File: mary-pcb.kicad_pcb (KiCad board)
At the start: 2 copper layers, 76.2 x 130.8 mm, 69 parts, among them SW1 SW_Push, SW2 Rotary_Encoder_Switch, U1 ATmega32U4-AU, Y1 16MHz

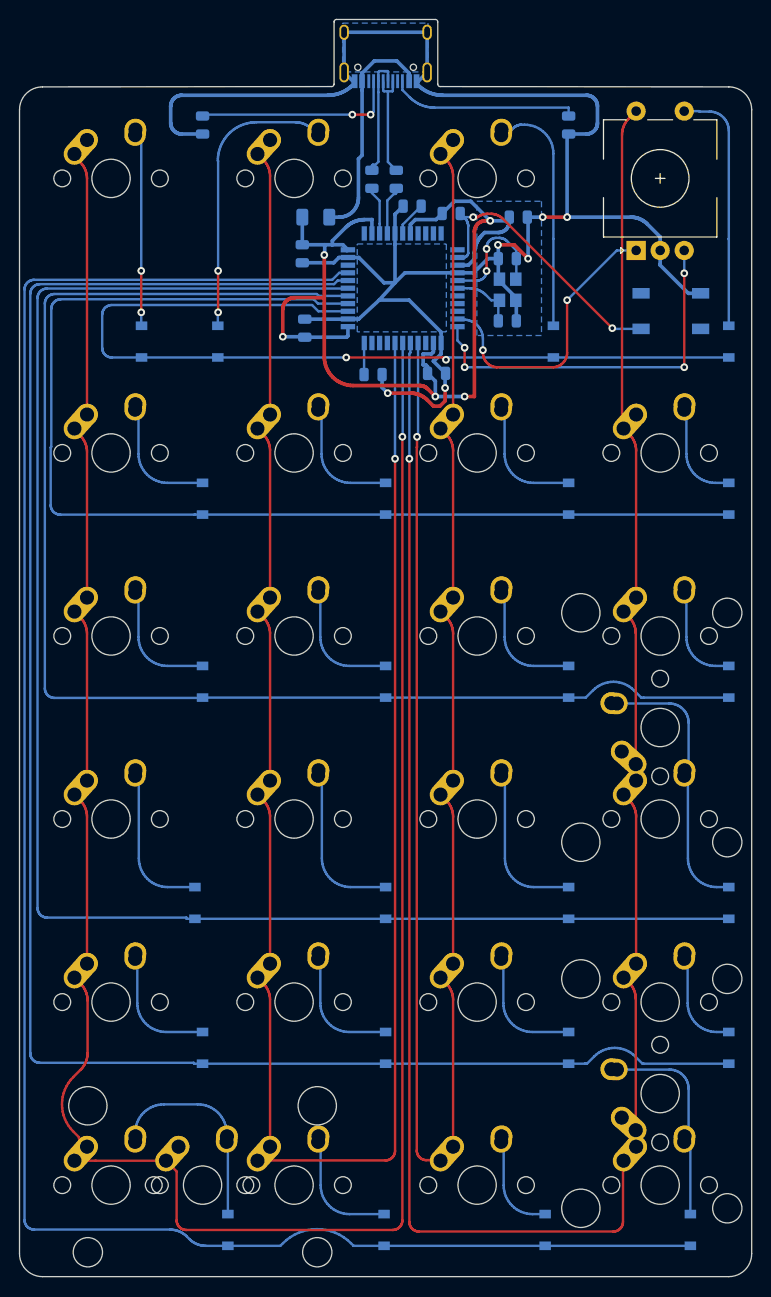
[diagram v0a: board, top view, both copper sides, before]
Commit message: add esd protection, ground pours, via stitching
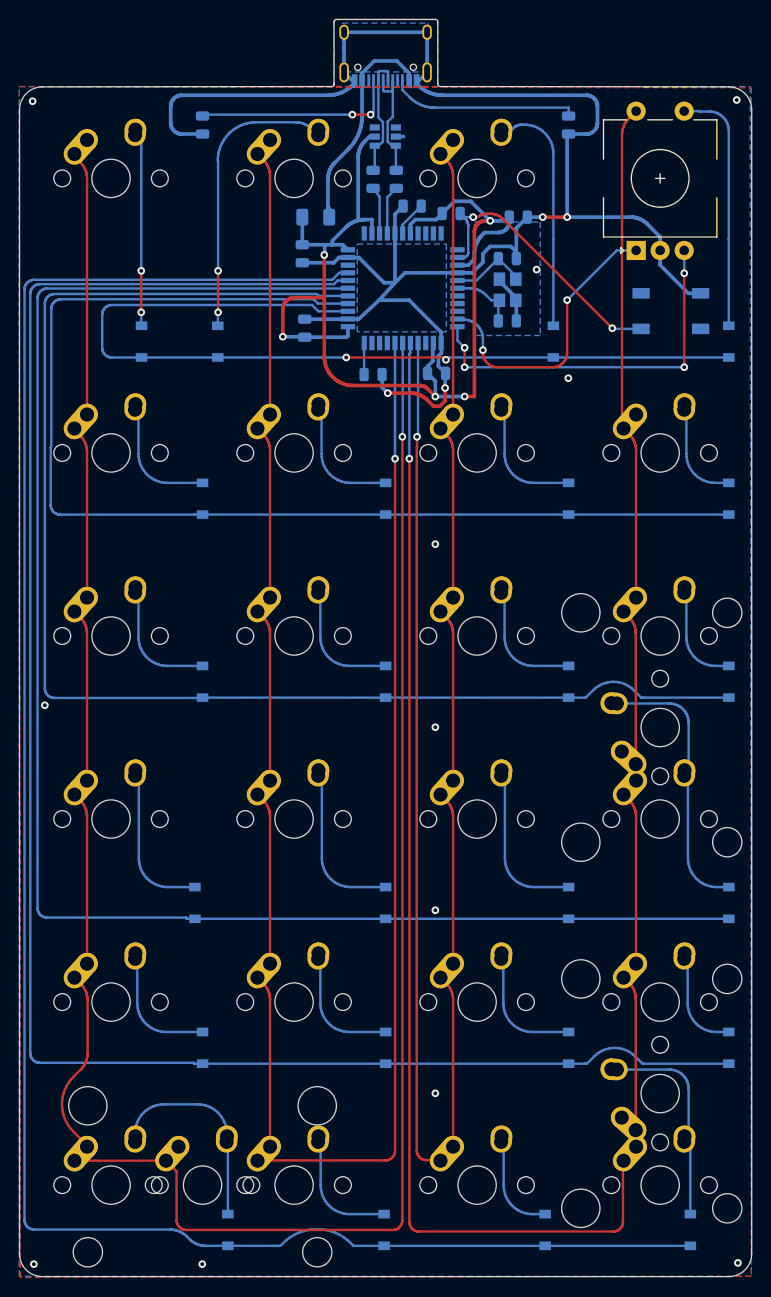
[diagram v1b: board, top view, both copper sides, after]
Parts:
- added U2: SRV05-4, Package_TO_SOT_SMD:SOT-23-6, B.Cu at (153.2, 37.7)
- moved R5 0.13 mm to (151.9, 42.2)
- turned C2 to 0 degrees
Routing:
- net +5V: track 108.7 -> 117.3 mm
- net Net-(C2-Pad1): track 13.3 -> 8.18 mm, vias 2 -> 0
- net GND: track 187.3 -> 184.8 mm, vias 6 -> 16
- net D+: track 11.6 -> 13.1 mm
- net VCC: track 24.1 -> 23.2 mm
- net D-: track 12.7 -> 13.6 mm
- added copper zone on F.Cu, net GND

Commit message: edit ground pours, via stitching, fuse placement
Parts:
- moved F1 11.1 mm to (149.4, 35.6), turned to 90 degrees
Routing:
- net VCC: track 23.2 -> 10.6 mm
- net GND: track 184.8 -> 190.9 mm, vias 16 -> 19
- net +5V: track 117.3 -> 121.9 mm
- net Net-(R2-Pad2): track 21.2 -> 21.1 mm, vias 2 -> 0

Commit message: fix drc error caused by via
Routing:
- net GND: track 190.9 -> 191.4 mm
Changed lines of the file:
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@@
     (tags capacitor)
     (attr smd)
-    (fp_text reference C2 (at 0 1.65) (layer B.SilkS)
+    (fp_text reference C2 (at 2.794 0) (layer B.SilkS)
       (effects (font (size 1 1) (thickness 0.15)) (justify mirror))
     )
@@
   (segment (start 144.526 50.8485) (end 147.794098 50.8485) (width 0.381) (layer B.Cu) (net 1))
   (segment (start 144.78 56.7205) (end 149.25 56.7205) (width 0.381) (layer B.Cu) (net 1))
-  (via (at 144.526 51.943) (size 0.8) (drill 0.4) (layers F.Cu B.Cu) (net 1))
-  (segment (start 144.526 51.943) (end 144.526 50.8485) (width 0.381) (layer B.Cu) (net 1))
   (via (at 143.51 56.007) (size 0.8) (drill 0.4) (layers F.Cu B.Cu) (net 1))
   (segment (start 143.51 56.007) (end 144.78 56.7205) (width 0.381) (layer B.Cu) (net 1))
@@
   (segment (start 155.956 43.561) (end 155.0185 44.958) (width 0.381) (layer B.Cu) (net 1))
   (segment (start 187.833 53.975) (end 185.98 54.03) (width 0.381) (layer B.Cu) (net 1))
+  (via (at 143.256 51.816) (size 0.8) (drill 0.4) (layers F.Cu B.Cu) (net 1))
+  (segment (start 143.256 51.816) (end 144.526 50.8485) (width 0.381) (layer B.Cu) (net 1))
   (segment (start 161.67575 53.49875) (end 160.67175 53.49875) (width 0.254) (layer B.Cu) (net 2))
   (segment (start 165.04375 54.7575) (end 164.18975 54.7575) (width 0.254) (layer B.Cu) (net 2))

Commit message: move usb
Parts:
- moved USB1 2.41 mm to (153.2, 26.7)
- moved F1 2.18 mm to (149.0, 37.7)
- moved U2 1.02 mm to (153.2, 38.7)
- moved C3 0.13 mm to (156.0, 45.1)
- moved R4 0.13 mm to (154.3, 42.3)
- moved R5 0.13 mm to (151.9, 42.3)
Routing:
- net GND: track 191.4 -> 189.0 mm, vias 19 -> 18
- net D+: track 13.1 -> 10.8 mm
- net D-: track 13.6 -> 11.3 mm
- net Net-(R2-Pad2): track 21.1 -> 19.7 mm, vias 0 -> 2
- net Net-(R3-Pad2): track 19.7 -> 20.4 mm
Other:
- board size 76.2 x 130.8 mm -> 76.2 x 128.2 mm
